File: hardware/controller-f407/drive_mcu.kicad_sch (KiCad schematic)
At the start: 12 parts, among them J10 SWD, J11 UART, U20 STM32G431RBTx

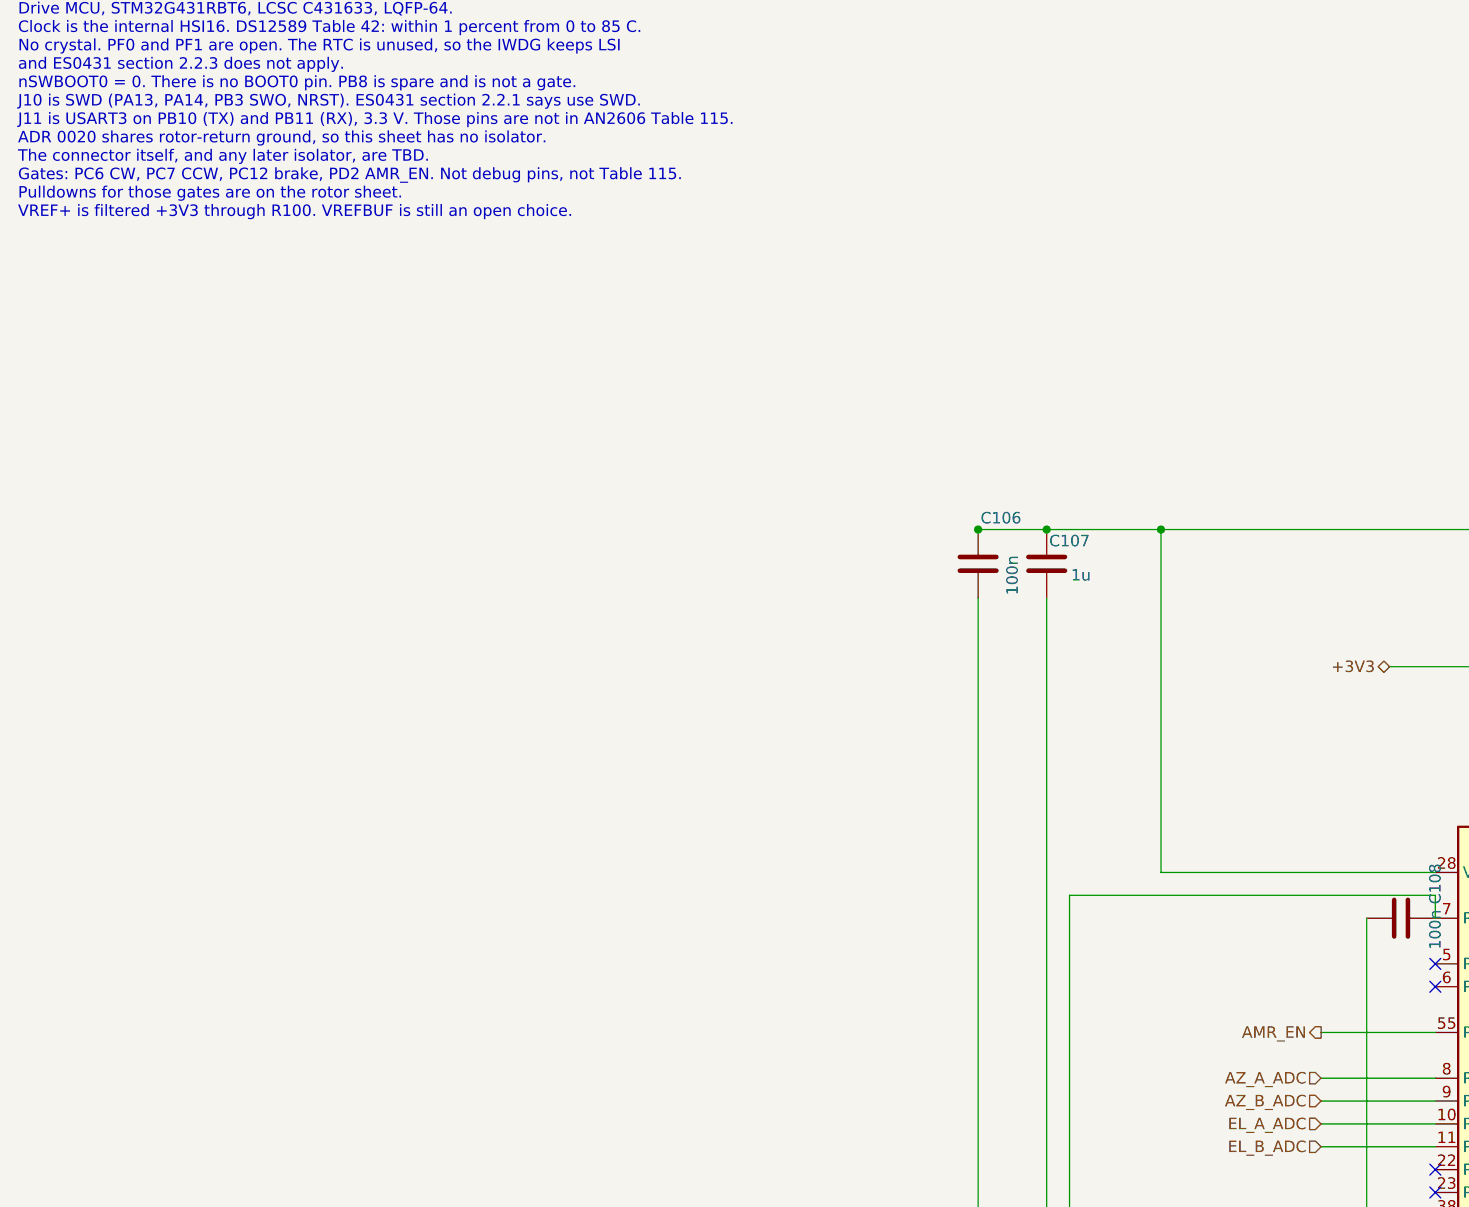
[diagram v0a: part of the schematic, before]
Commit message: Rename the relay net back to ARM_EN and drop the dangling stub.
The owner's label text is ARM_EN again, in place. One pulldown remains
on each gate line. TR1 conditioning stays on the rotor sheet.

Co-authored-by: Jeffrey Millar <wa1hco@users.noreply.github.com>
Co-authored-by: Cursor Agent <cursoragent@cursor.com>
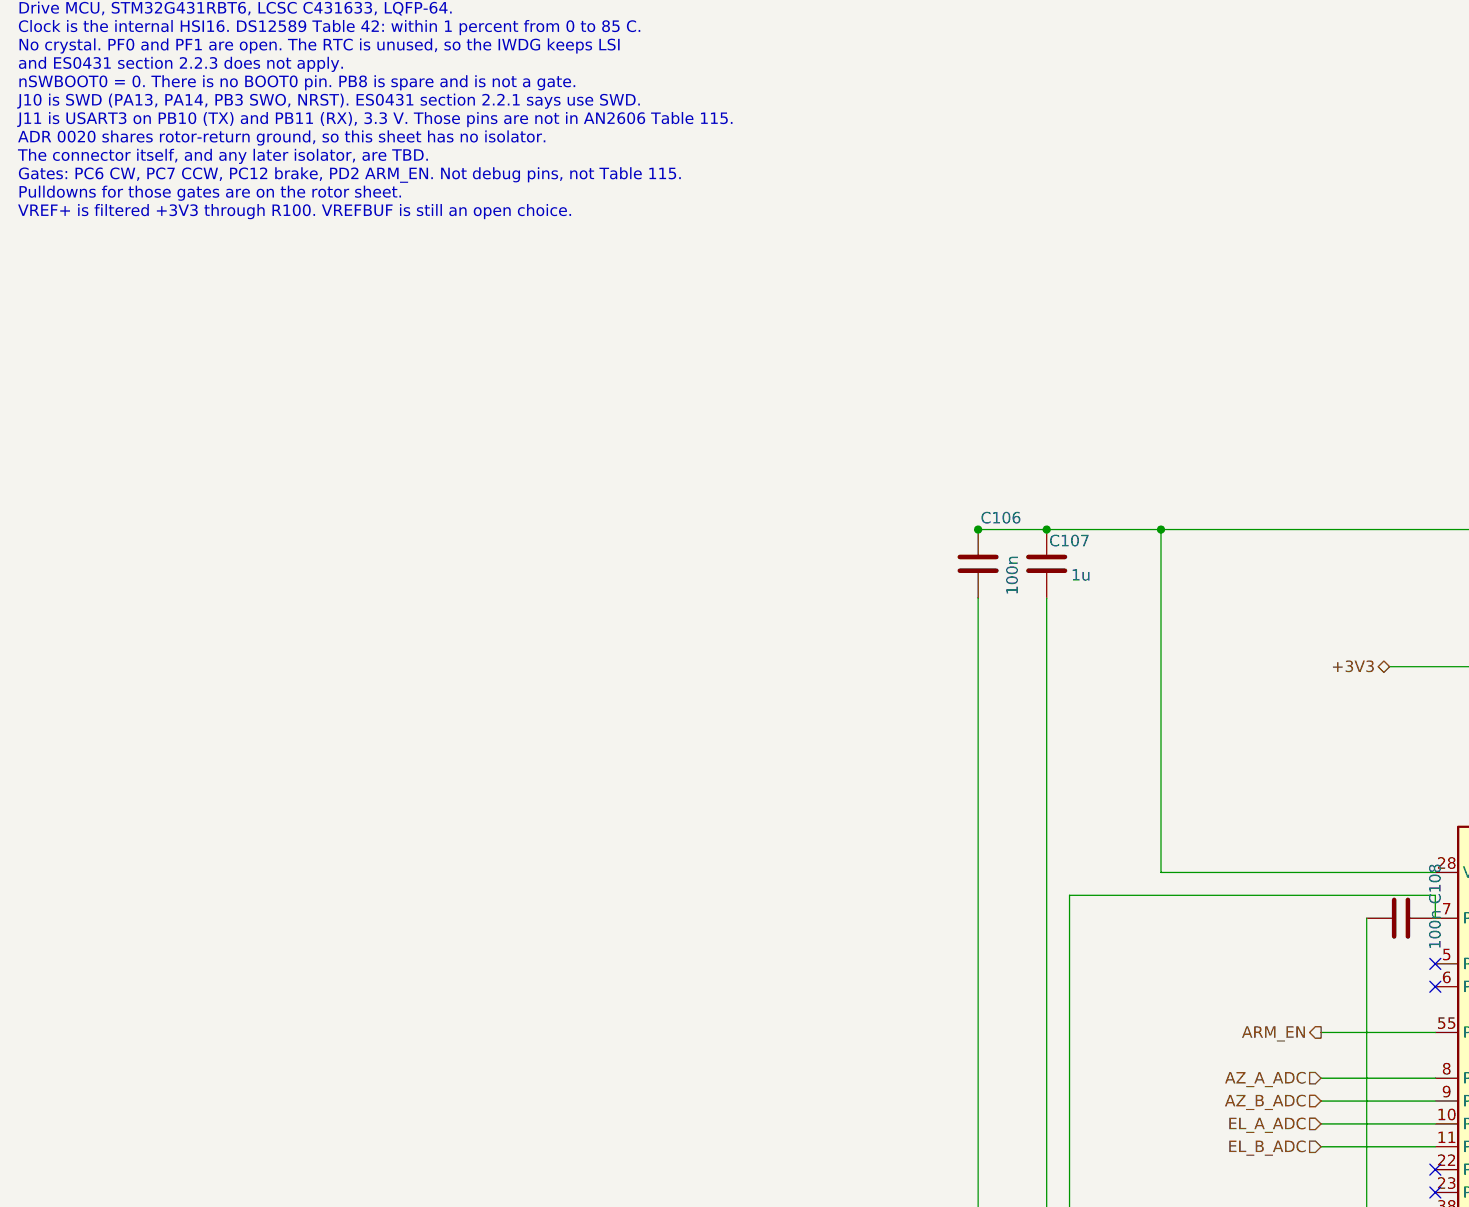
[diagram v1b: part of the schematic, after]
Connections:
- net AMR_EN renamed ARM_EN
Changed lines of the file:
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@@
 	(hierarchical_label "AZ_CCW_EN" (shape output) (at 160.02 152.4 180) (effects (font (size 1.27 1.27)) (justify right)))
 	(hierarchical_label "AZ_BRAKE_EN" (shape output) (at 160.02 165.1 180) (effects (font (size 1.27 1.27)) (justify right)))
-	(hierarchical_label "AMR_EN" (shape output) (at 160.02 129.54 180) (effects (font (size 1.27 1.27)) (justify right)))
+	(hierarchical_label "ARM_EN" (shape output) (at 160.02 129.54 180) (effects (font (size 1.27 1.27)) (justify right)))
 	(hierarchical_label "AZ_CW_SNS" (shape input) (at 160.02 167.64 180) (effects (font (size 1.27 1.27)) (justify right)))
 	(hierarchical_label "AZ_CCW_SNS" (shape input) (at 160.02 170.18 180) (effects (font (size 1.27 1.27)) (justify right)))
@@
 		)
 	)
-	(text "Drive MCU, STM32G431RBT6, LCSC C431633, LQFP-64.\nClock is the internal HSI16. DS12589 Table 42: within 1 percent from 0 to 85 C.\nNo crystal. PF0 and PF1 are open. The RTC is unused, so the IWDG keeps LSI\nand ES0431 section 2.2.3 does not apply.\nnSWBOOT0 = 0. There is no BOOT0 pin. PB8 is spare and is not a gate.\nJ10 is SWD (PA13, PA14, PB3 SWO, NRST). ES0431 section 2.2.1 says use SWD.\nJ11 is USART3 on PB10 (TX) and PB11 (RX), 3.3 V. Those pins are not in AN2606 Table 115.\nADR 0020 shares rotor-return ground, so this sheet has no isolator.\nThe connector itself, and any later isolator, are TBD.\nGates: PC6 CW, PC7 CCW, PC12 brake, PD2 AMR_EN. Not debug pins, not Table 115.\nPulldowns for those gates are on the rotor sheet.\nVREF+ is filtered +3V3 through R100. VREFBUF is still an open choice." (exclude_from_sim no) (at 15.24 15.24 0) (effects (font (size 1.27 1.27)) (justify left top)))
+	(text "Drive MCU, STM32G431RBT6, LCSC C431633, LQFP-64.\nClock is the internal HSI16. DS12589 Table 42: within 1 percent from 0 to 85 C.\nNo crystal. PF0 and PF1 are open. The RTC is unused, so the IWDG keeps LSI\nand ES0431 section 2.2.3 does not apply.\nnSWBOOT0 = 0. There is no BOOT0 pin. PB8 is spare and is not a gate.\nJ10 is SWD (PA13, PA14, PB3 SWO, NRST). ES0431 section 2.2.1 says use SWD.\nJ11 is USART3 on PB10 (TX) and PB11 (RX), 3.3 V. Those pins are not in AN2606 Table 115.\nADR 0020 shares rotor-return ground, so this sheet has no isolator.\nThe connector itself, and any later isolator, are TBD.\nGates: PC6 CW, PC7 CCW, PC12 brake, PD2 ARM_EN. Not debug pins, not Table 115.\nPulldowns for those gates are on the rotor sheet.\nVREF+ is filtered +3V3 through R100. VREFBUF is still an open choice." (exclude_from_sim no) (at 15.24 15.24 0) (effects (font (size 1.27 1.27)) (justify left top)))
 	(embedded_fonts no)
 )
